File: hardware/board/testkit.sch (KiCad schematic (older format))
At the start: 3 parts, among them J5 Left, J6 Right, J7 Bottom

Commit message: Re-do the motherboard
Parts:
- added J4, J8, J9: EXT, Connector_Wire:SolderWire-0.75sqmm_1x06_P4.8mm_D1.25mm_OD2.3mm, symbol Connector_Generic:Conn_01x06
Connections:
- net A13 is gone; now on net GND: J5.29 (Pin_29)
- net A14 is gone; now on net GND: J5.30 (Pin_30)
- net A5-PRE is gone; now on net GND: J5.19 (Pin_19)
- net A6-PRE is gone; now on net GND: J5.20 (Pin_20)
- net DB0 is gone; now on net GND: J7.19 (Pin_19)
- net DR1 is gone; now on net DAC_2B: J7.37 (Pin_37)
- net DR2 is gone; now on net DAC_2D: J7.35 (Pin_35)
- net DR3 is gone; now on net DAC_3B: J7.33 (Pin_33)
- net DR4 is gone; now on net DAC_3D: J7.31 (Pin_31)
- net OSC_A is gone; now on net GND: J6.18 (Pin_18)
- net OSC_B is gone; now on net GND: J6.17 (Pin_17)
- net +12VDOWNSTREAM: now also J5.5 (Pin_5); no longer J5.4 (Pin_4)
- net -12VDOWNSTREAM: now also J5.4 (Pin_4), J5.6 (Pin_6); no longer J5.7 (Pin_7), J5.8 (Pin_8)
- net DAC_1A: now also J6.32 (Pin_32); no longer J6.26 (Pin_26)
- net DAC_1B: now also J6.31 (Pin_31); no longer J6.25 (Pin_25)
- net DAC_1C: now also J6.34 (Pin_34); no longer J6.27 (Pin_27)
- net DAC_1D: now also J6.33 (Pin_33); no longer J6.28 (Pin_28)
- net DAC_2A: now also J7.38 (Pin_38); no longer J6.22 (Pin_22)
- net DAC_2B: no longer J6.21 (Pin_21)
- net DAC_2C: now also J7.36 (Pin_36); no longer J6.23 (Pin_23)
- net DAC_2D: no longer J6.24 (Pin_24)
- net DAC_3A: now also J7.34 (Pin_34); no longer J6.36 (Pin_36)
- net DAC_3B: no longer J6.35 (Pin_35)
- net DAC_3C: now also J7.32 (Pin_32); no longer J6.37 (Pin_37)
- net DAC_3D: no longer J6.38 (Pin_38)
- net DAC_4A: now also J6.36 (Pin_36); no longer J6.32 (Pin_32)
- net DAC_4B: now also J6.35 (Pin_35); no longer J6.31 (Pin_31)
- net DAC_4C: now also J6.38 (Pin_38); no longer J6.33 (Pin_33)
- net DAC_4D: now also J6.37 (Pin_37); no longer J6.34 (Pin_34)
- net GND: now also J6.24 (Pin_24), J7.11 (Pin_11), J7.17 (Pin_17), J7.29 (Pin_29), J4.1 (Pin_1), J4.6 (Pin_6), J8.1 (Pin_1), J8.6 (Pin_6); no longer J5.27 (Pin_27), J5.28 (Pin_28), J5.5 (Pin_5), J5.6 (Pin_6), J6.13 (Pin_13), J6.14 (Pin_14), J6.19 (Pin_19), J6.20 (Pin_20), J7.10 (Pin_10), J7.14 (Pin_14), J7.16 (Pin_16), J7.21 (Pin_21), J7.22 (Pin_22), J7.24 (Pin_24), J7.26 (Pin_26), J7.3 (Pin_3), J7.32 (Pin_32), J7.34 (Pin_34), J7.36 (Pin_36), J7.38 (Pin_38), J7.4 (Pin_4), J7.5 (Pin_5), J7.6 (Pin_6), J7.8 (Pin_8)
- net SERIAL1.0: now also J6.28 (Pin_28); no longer J7.23 (Pin_23)
- net SERIAL1.1: now also J6.27 (Pin_27); no longer J7.25 (Pin_25)
- net SERIAL1.2: now also J6.26 (Pin_26); no longer J7.27 (Pin_27)
- net SERIAL1.3: now also J6.25 (Pin_25); no longer J7.29 (Pin_29)
- net SERIAL4.0: now also J7.24 (Pin_24); no longer J7.11 (Pin_11)
- net SERIAL4.1: now also J7.23 (Pin_23); no longer J7.13 (Pin_13)
- net SERIAL4.2: now also J7.26 (Pin_26); no longer J7.15 (Pin_15)
- net SERIAL4.3: now also J7.25 (Pin_25); no longer J7.17 (Pin_17)
- net ADC_2D: now reaches J5.37 (Pin_37)
- net ADC_2C: now reaches J5.38 (Pin_38)
- net A1-PRE renamed IO22
- net A10-PRE renamed ADC_1C
- net A11-PRE renamed ADC_4B
- net A12-PRE renamed ADC_4A
- net A15 renamed ADC_3B
- net A16 renamed ADC_3A
- net A17 renamed ADC_3C
- net A18 renamed ADC_3D
- net A19 renamed ADC_2A
- net A2-PRE renamed IO23
- net A20 renamed ADC_2B
- net A3-PRE renamed IO20
- net A4-PRE renamed IO21
- net A7-PRE renamed ADC_1B
- net A8-PRE renamed ADC_1A
- net A9-PRE renamed ADC_1D
- net AUDIO_IN_1A renamed EXT_MM_A
- net EXT_MM_A: now also J4.3 (Pin_3)
- net AUDIO_IN_1B renamed EXT_MM_V
- net EXT_MM_V: now also J4.2 (Pin_2)
- net AUDIO_IN_1C renamed EXT_FG_A
- net EXT_FG_A: now also J9.5 (Pin_5)
- net AUDIO_IN_1D renamed EXT_FG_B
- net EXT_FG_B: now also J9.6 (Pin_6)
- net AUDIO_IN_2A renamed EXT_OSC_C
- net EXT_OSC_C: now also J8.3 (Pin_3)
- net AUDIO_IN_2B renamed EXT_OSC_D
- net EXT_OSC_D: now also J8.2 (Pin_2)
- net AUDIO_IN_2C renamed EXT_AUDIO_A
- net EXT_AUDIO_A: now also J4.4 (Pin_4)
- net AUDIO_IN_2D renamed EXT_AUDIO_B
- net EXT_AUDIO_B: now also J4.5 (Pin_5)
- net AUDIO_OUT_L renamed EXT_OSC_A
- net EXT_OSC_A: now also J8.5 (Pin_5)
- net AUDIO_OUT_R renamed EXT_OSC_B
- net EXT_OSC_B: now also J8.4 (Pin_4)
- net DB1 renamed IO15
- net DB2 renamed IO13
- net OSC_C renamed EXT_INST_C
- net EXT_INST_C: now also J9.2 (Pin_2)
- net OSC_D renamed EXT_INST_D
- net EXT_INST_D: now also J9.1 (Pin_1)
- new net +12V: J5.7 (Pin_7)
- new net -12V: J5.8 (Pin_8)
- new net ADC_4C: J5.28 (Pin_28)
- new net ADC_4D: J5.27 (Pin_27)
- new net EXT_INST_A: J6.13 (Pin_13), J9.3 (Pin_3)
- new net EXT_INST_B: J6.14 (Pin_14), J9.4 (Pin_4)
- new net IO1: J6.19 (Pin_19)
- new net IO10: J7.16 (Pin_16)
- new net IO11: J7.13 (Pin_13)
- new net IO12: J7.14 (Pin_14)
- new net IO14: J7.10 (Pin_10)
- new net IO16: J7.8 (Pin_8)
- new net IO17: J7.5 (Pin_5)
- new net IO18: J7.6 (Pin_6)
- new net IO19: J7.3 (Pin_3)
- new net IO2: J6.20 (Pin_20)
- new net IO3: J6.21 (Pin_21)
- new net IO4: J6.22 (Pin_22)
- new net IO5: J6.23 (Pin_23)
- new net IO6: J7.27 (Pin_27)
- new net IO7: J7.21 (Pin_21)
- new net IO8: J7.22 (Pin_22)
- new net IO9: J7.15 (Pin_15)
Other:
- note removed: "TODO: Wire up CS :("
- moved on the sheet: J5, J6, J7

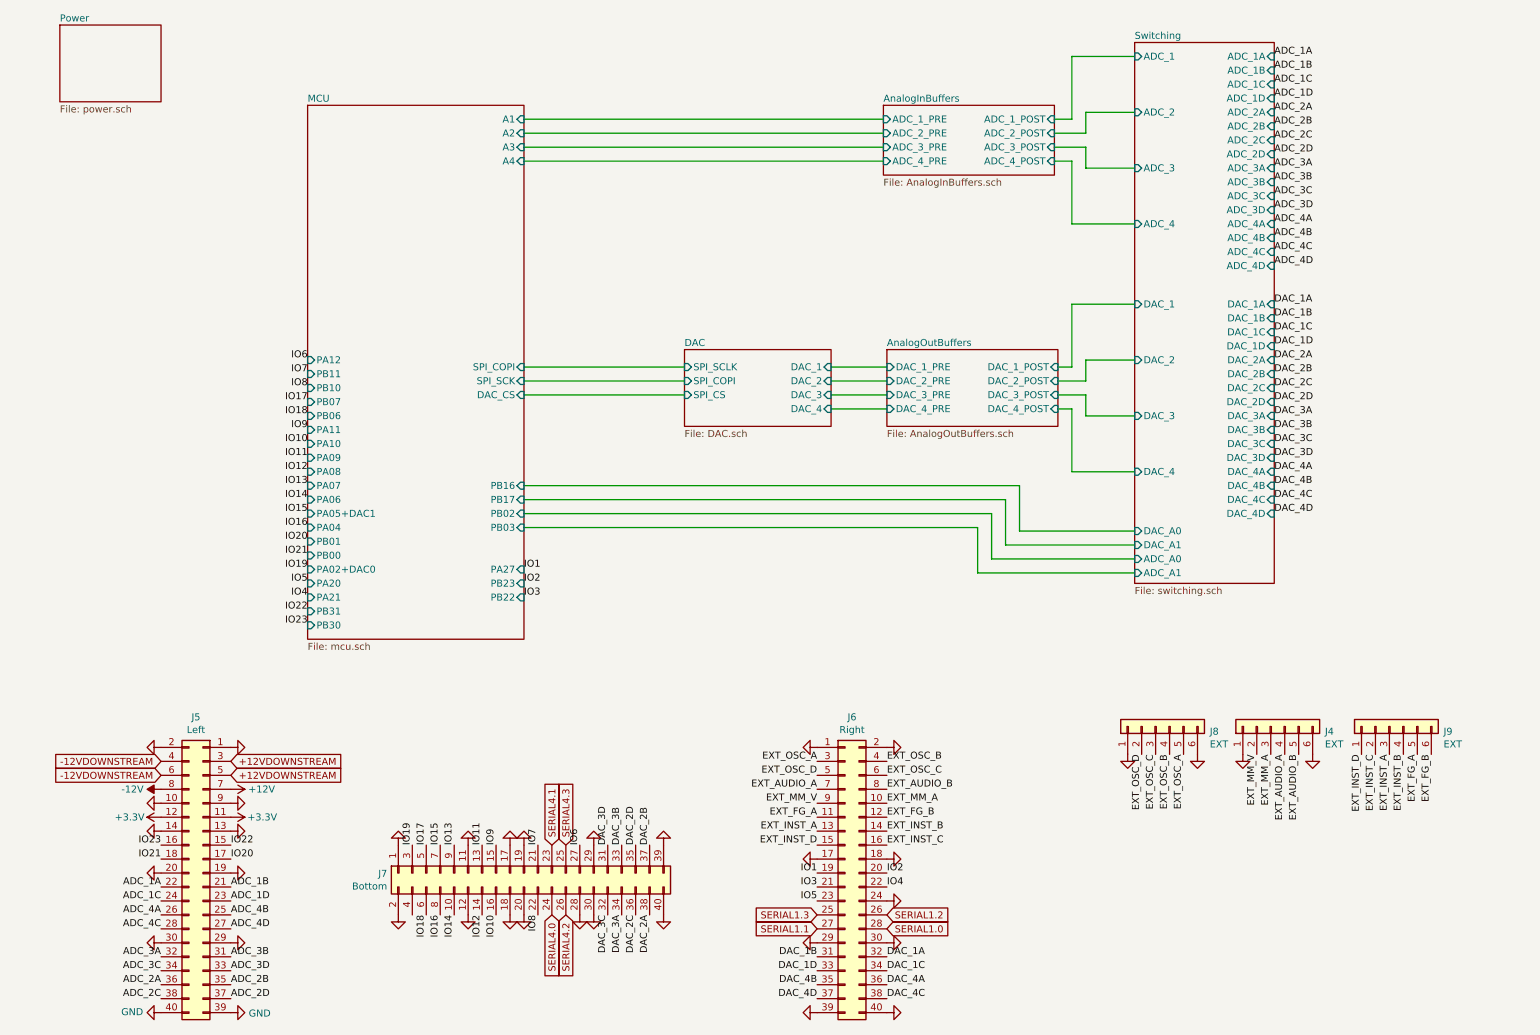
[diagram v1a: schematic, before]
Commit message: Fix issues found in hardware v1
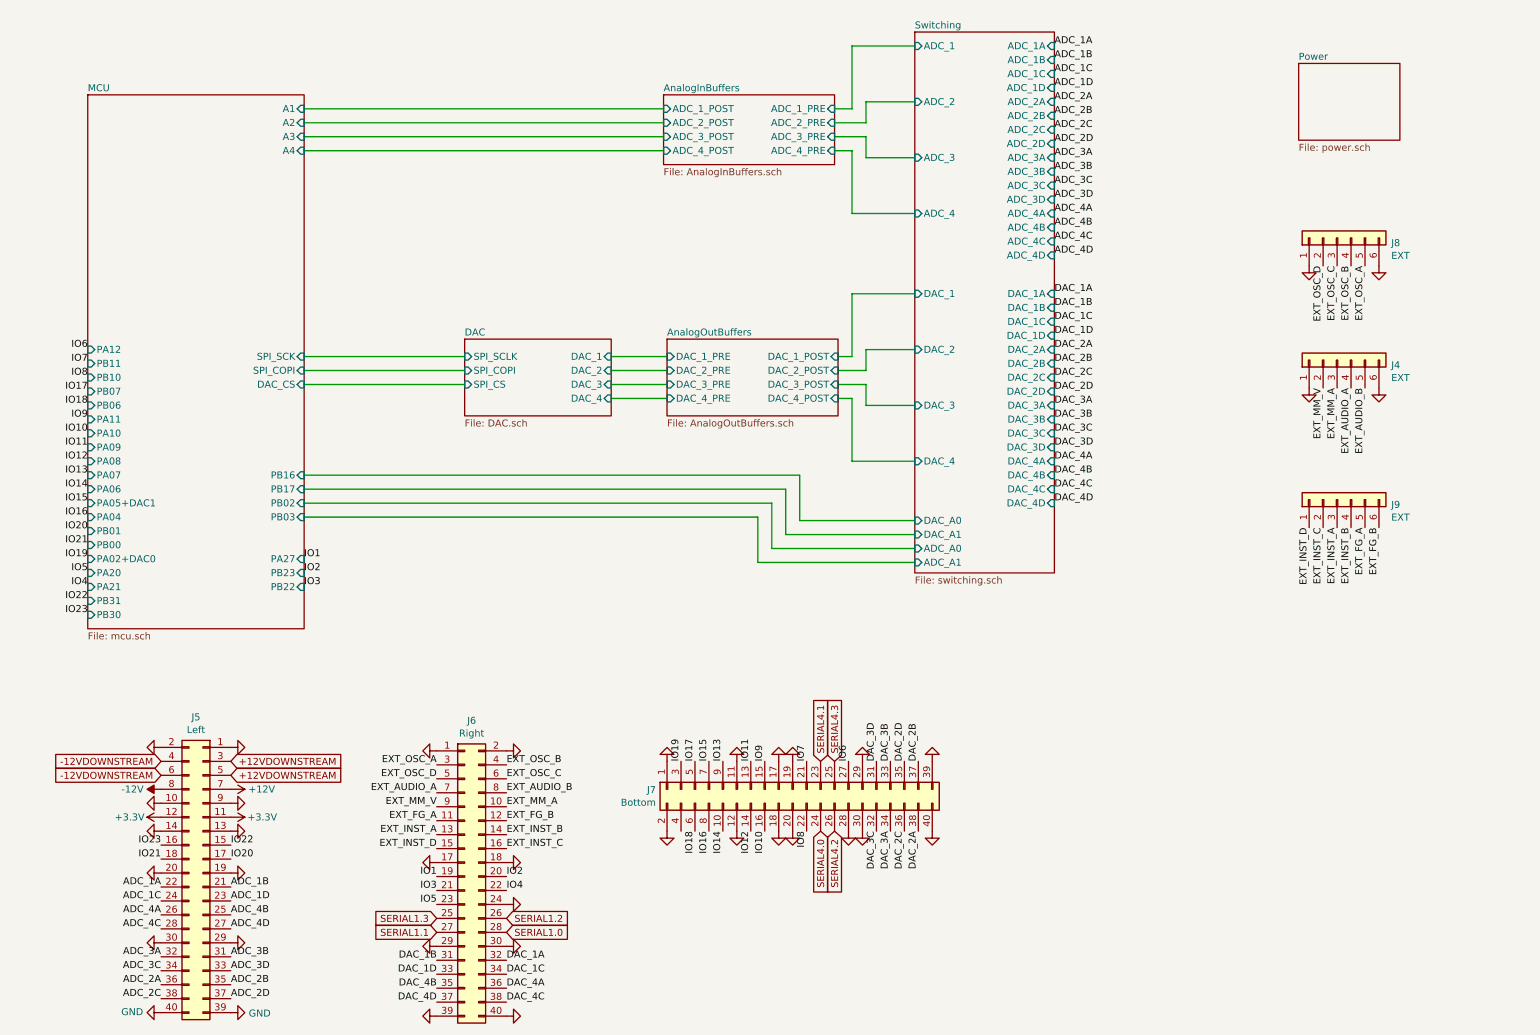
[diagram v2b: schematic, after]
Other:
- moved on the sheet: J4, J6, J7, J8, J9
